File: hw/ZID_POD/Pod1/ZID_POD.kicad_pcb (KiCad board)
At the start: 2 copper layers, 52.8 x 19.3 mm, 2 parts, among them J1 Z80-POD (1)

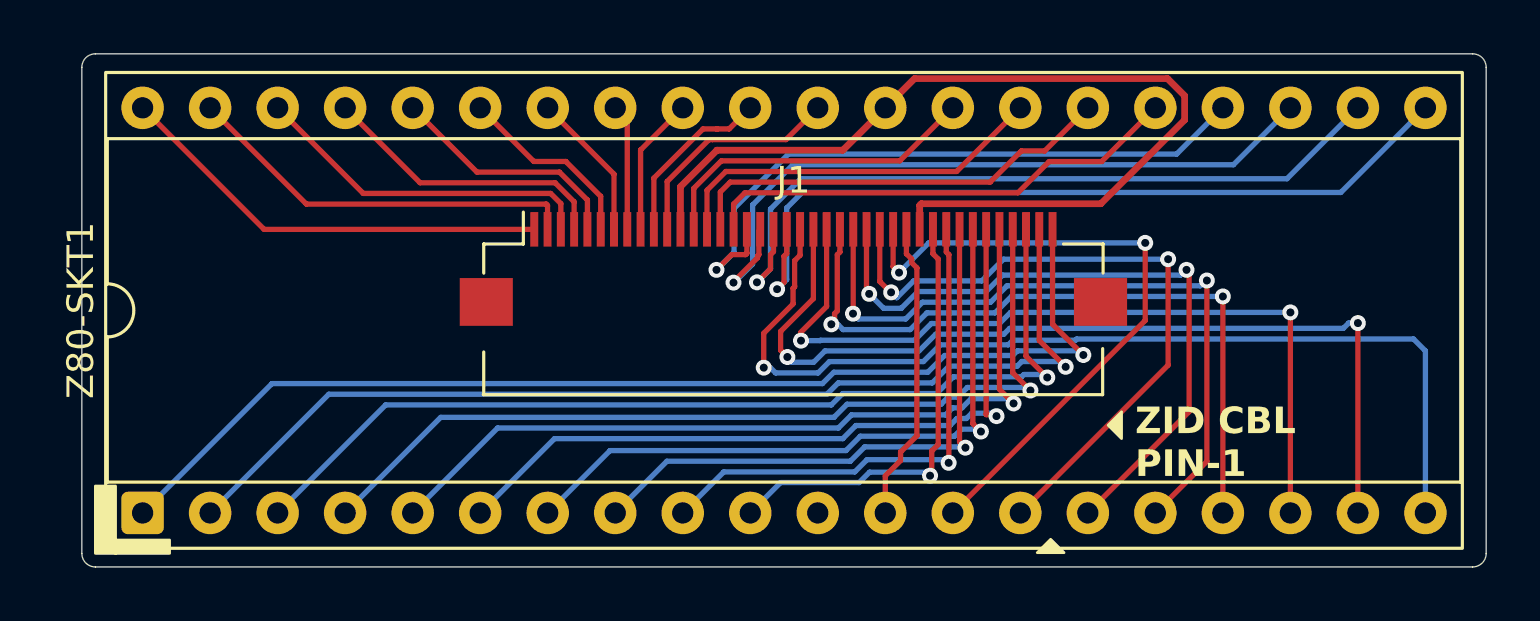
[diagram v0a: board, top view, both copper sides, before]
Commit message: PCB: Ready to order - ZID, POD1, POD2, POD3, POD4, ExpBP
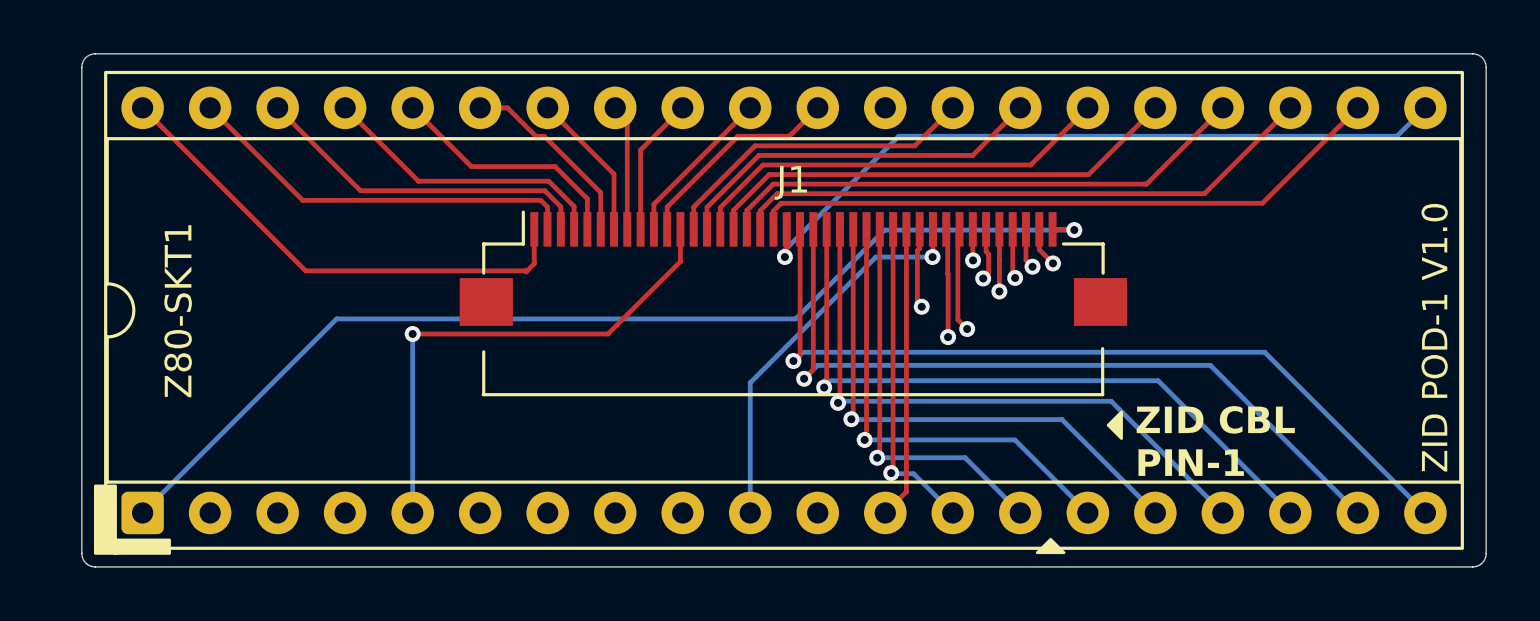
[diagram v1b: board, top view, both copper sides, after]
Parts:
- J1: value Z80-POD (1) -> FFC/FPC-40 Socket
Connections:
- J1 pad 12: /GND -> /A15
- J1 pad 30: /GND -> /D4
- J1 pad 34: /D4 -> /GND
- J1 pad 36: /A15 -> /GND
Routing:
- net /GND: track 35.6 -> 3.51 mm, vias 0 -> 2
- net /D7: track 24.6 -> 12.1 mm, vias 2 -> 1
- net /A15: track 31.2 -> 19.1 mm
- net /D0: track 25.5 -> 14.9 mm, vias 2 -> 1
- net /D1: track 26.0 -> 17.5 mm, vias 2 -> 1
- net /INT-: track 26.7 -> 20.1 mm, vias 2 -> 1
- net /IORQ-: track 37.6 -> 31.5 mm
- net /MREQ-: track 34.7 -> 29.1 mm, vias 2 -> 1
- net /HALT-: track 31.0 -> 25.8 mm, vias 2 -> 1
- net /BACK-: track 27.3 -> 22.3 mm, vias 1 -> 0
- net /D4: track 25.4 -> 20.3 mm
- net /WAIT-: track 24.8 -> 20.2 mm, vias 1 -> 0
- net /WR-: track 28.9 -> 24.3 mm, vias 1 -> 0
- net /NMI-: track 27.2 -> 22.8 mm, vias 2 -> 1
- net /CLK: track 28.4 -> 24.5 mm
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- added copper zone on In1.Cu, net /GND
- added copper zone on In2.Cu, net /GND
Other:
- copper layers 2 -> 4
- board text added: "ZID POD-1 V1.0"
